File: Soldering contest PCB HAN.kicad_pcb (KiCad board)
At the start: 2 copper layers, 11 parts, among them J1 Screw_Terminal_01x02, Q1 2N3904, Q2 2N3904

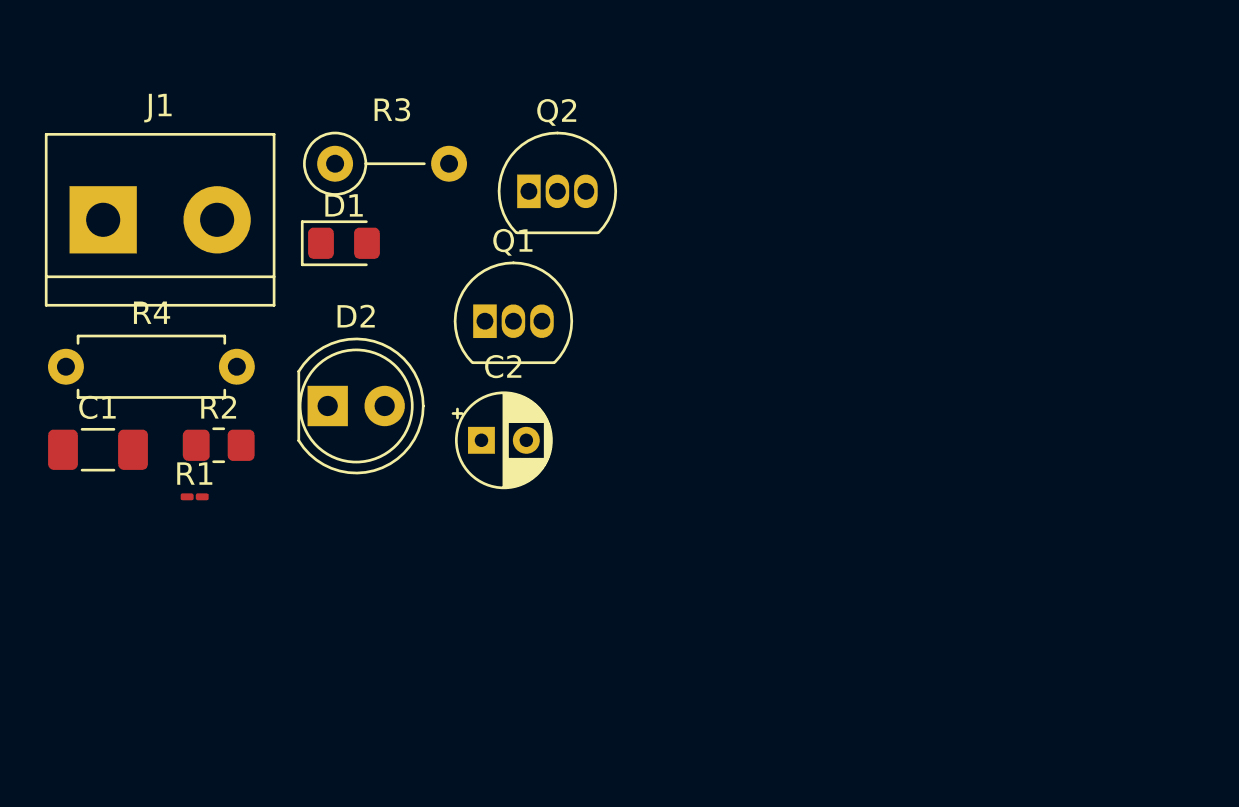
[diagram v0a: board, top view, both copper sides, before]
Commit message: replaced q1 footprint
replaced with sot23 handsolderable
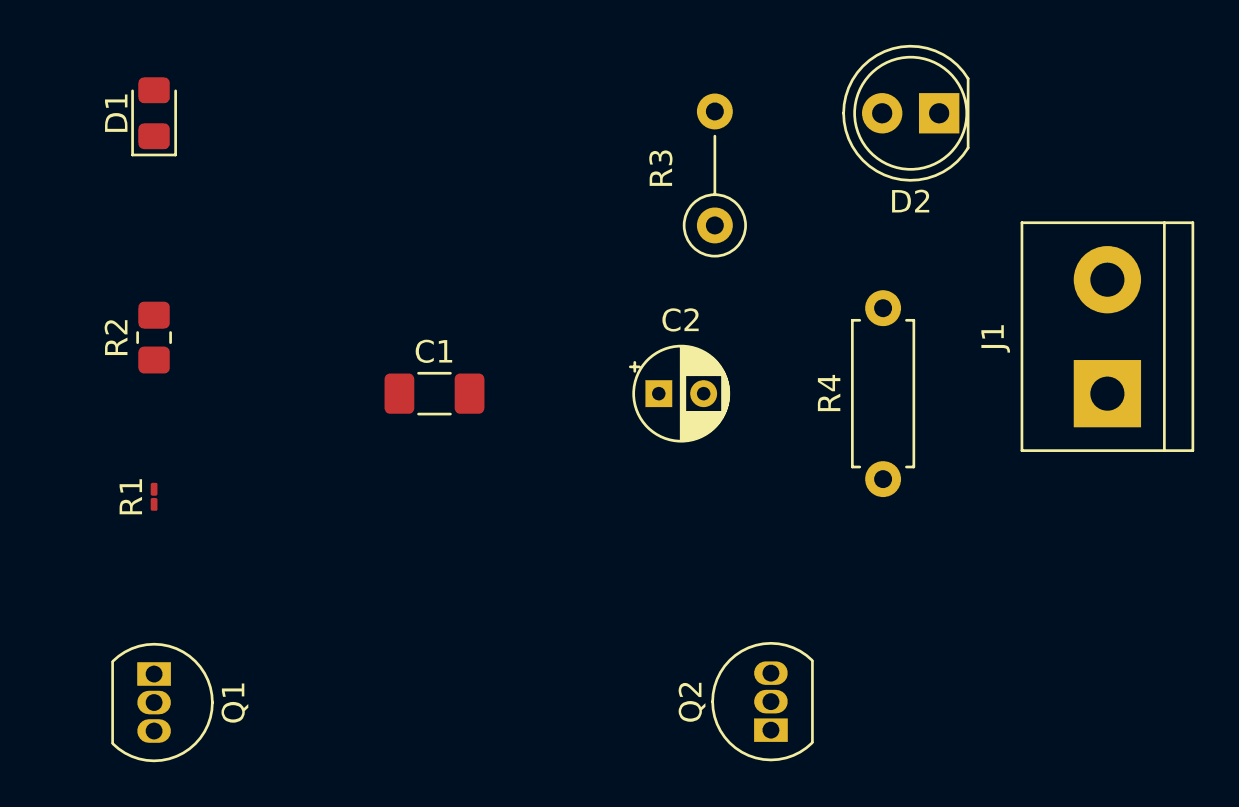
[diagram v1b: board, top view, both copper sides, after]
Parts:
- moved J1 45.4 mm to (175.0, 97.5), turned to 90 degrees
- moved R4 36.8 mm to (165.0, 101.3), turned to 90 degrees
- moved D2 30.2 mm to (167.5, 85.0), turned to 180 degrees
- moved Q2 26.3 mm to (160.0, 112.5), turned to 90 degrees
- moved Q1 21.6 mm to (132.5, 110.0), turned to -90 degrees
- moved R3 17.2 mm to (157.5, 90.0), turned to 90 degrees
- moved C1 15.2 mm to (145.0, 97.5)
- moved D1 10.3 mm to (132.5, 85.0), turned to 90 degrees
- moved C2 8.17 mm to (155.0, 97.5)
- moved R2 5.60 mm to (132.5, 95.0), turned to 90 degrees
- moved R1 1.81 mm to (132.5, 102.1), turned to 90 degrees

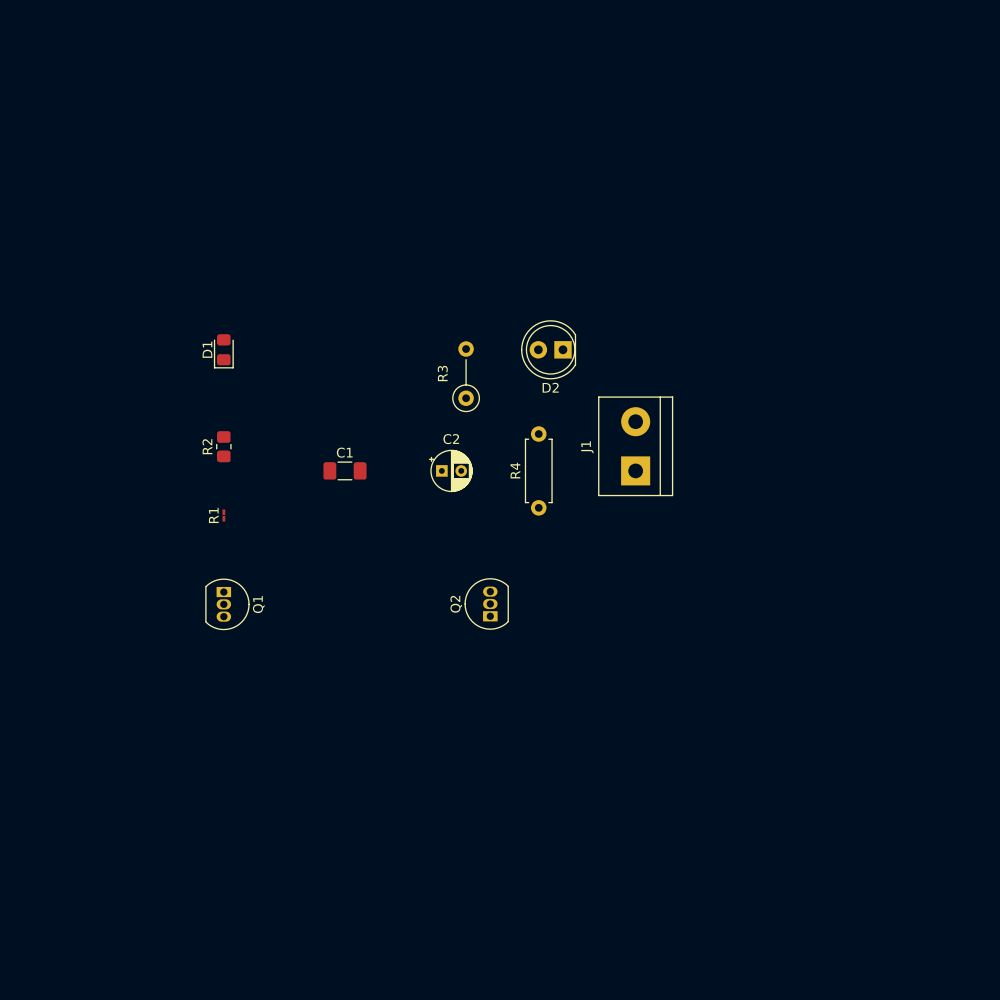
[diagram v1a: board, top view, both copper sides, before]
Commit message: archived 3d model, created general layout
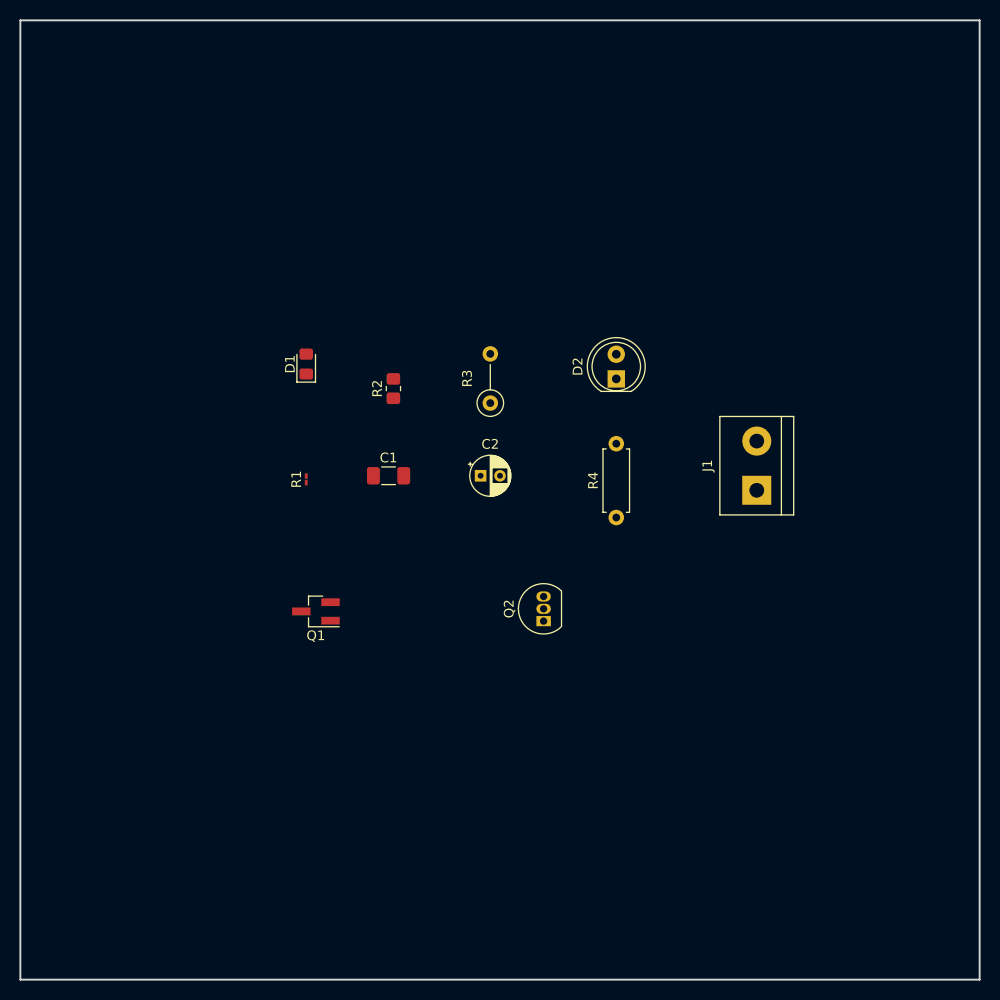
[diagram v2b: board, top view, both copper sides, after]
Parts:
- Q1: footprint Package_TO_SOT_THT:TO-92_Inline -> Package_TO_SOT_SMD:SOT-23_Handsoldering
- moved R2 18.5 mm to (150.0, 89.0)
- moved J1 12.7 mm to (187.5, 99.5)
- moved Q1 9.71 mm to (142.0, 112.0), turned to 180 degrees
- moved R1 9.29 mm to (141.0, 98.4)
- moved D1 8.63 mm to (141.0, 86.5)
- moved R4 8.06 mm to (173.0, 102.3)
- moved D2 6.26 mm to (173.0, 88.0), turned to 90 degrees
- moved Q2 5.52 mm to (165.5, 113.0)
- moved C1 4.53 mm to (149.5, 98.0)
- moved C2 4.03 mm to (159.0, 98.0)
- moved R3 2.55 mm to (160.0, 90.5)
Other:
- board outline added: 99 x 99 mm

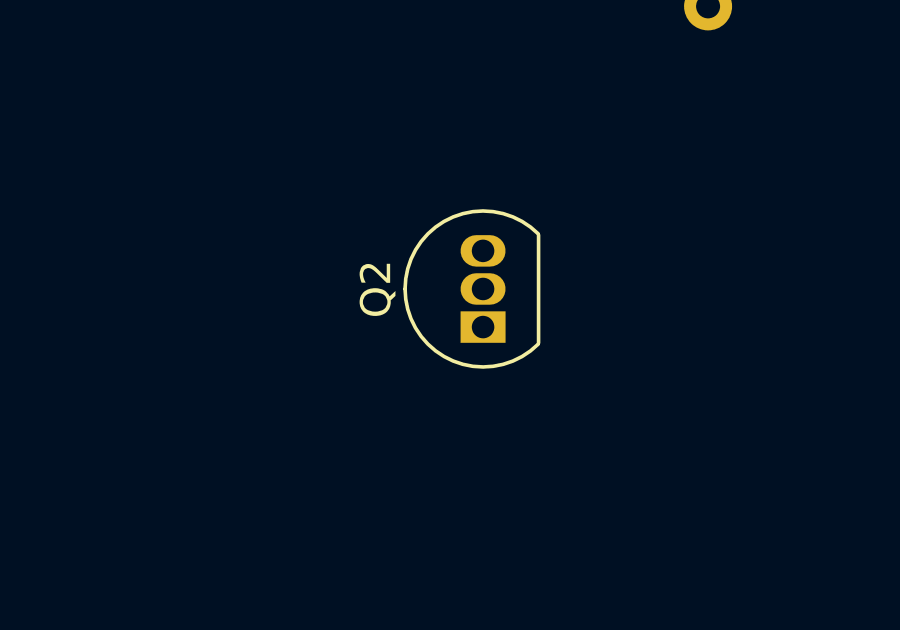
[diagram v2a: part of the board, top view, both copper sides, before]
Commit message: changed Q2 footprint
to to92 wide
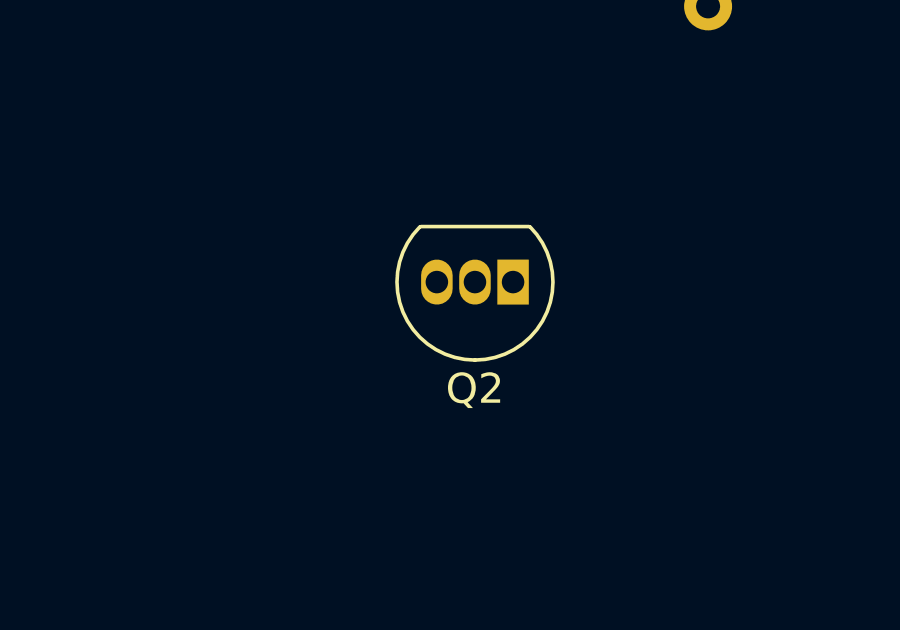
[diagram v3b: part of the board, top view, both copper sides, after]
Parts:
- moved Q2 1.80 mm to (166.5, 111.5), turned to 180 degrees
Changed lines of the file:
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@@
   )
   (footprint "Package_TO_SOT_THT:TO-92_Inline" (layer "F.Cu")
-    (at 165.5 113 90)
+    (at 166.5 111.5 180)
     (descr "TO-92 leads in-line, narrow, oval pads, drill 0.75mm (see NXP sot054_po.pdf)")
     (tags "to-92 sc-43 sc-43a sot54 PA33 transistor")
@@
     (property "Sheetname" "")
     (attr through_hole)
-    (fp_text reference "Q2" (at 1.27 -3.56 90) (layer "F.SilkS")
+    (fp_text reference "Q2" (at 1.27 -3.56) (layer "F.SilkS")
       (effects (font (size 1 1) (thickness 0.15)))
     )
-    (fp_text value "2N3904" (at 1.27 2.79 90) (layer "F.Fab")
+    (fp_text value "2N3904" (at 1.27 2.79) (layer "F.Fab")
       (effects (font (size 1 1) (thickness 0.15)))
     )
-    (fp_text user "${REFERENCE}" (at 1.27 0 90) (layer "F.Fab")
+    (fp_text user "${REFERENCE}" (at 1.27 0) (layer "F.Fab")
       (effects (font (size 1 1) (thickness 0.15)))
     )
@@
     (fp_arc (start 1.27 -2.48) (mid 3.561221 -0.949055) (end 3.023625 1.753625) (layer "F.Fab") (width 0.1))
     (fp_arc (start -0.483625 1.753625) (mid -1.021221 -0.949055) (end 1.27 -2.48) (layer "F.Fab") (width 0.1))
-    (pad "1" thru_hole rect (at 0 0 90) (size 1.05 1.5) (drill 0.75) (layers *.Cu *.Mask)
+    (pad "1" thru_hole rect (at 0 0 180) (size 1.05 1.5) (drill 0.75) (layers *.Cu *.Mask)
       (net 8 "GND") (pinfunction "E") (pintype "passive"))
-    (pad "2" thru_hole oval (at 1.27 0 90) (size 1.05 1.5) (drill 0.75) (layers *.Cu *.Mask)
+    (pad "2" thru_hole oval (at 1.27 0 180) (size 1.05 1.5) (drill 0.75) (layers *.Cu *.Mask)
       (net 2 "Net-(C1-Pad2)") (pinfunction "B") (pintype "passive"))
-    (pad "3" thru_hole oval (at 2.54 0 90) (size 1.05 1.5) (drill 0.75) (layers *.Cu *.Mask)
+    (pad "3" thru_hole oval (at 2.54 0 180) (size 1.05 1.5) (drill 0.75) (layers *.Cu *.Mask)
       (net 3 "Net-(C2-Pad1)") (pinfunction "C") (pintype "passive"))
     (model "${KIPRJMOD}/packages3D/TO-92_Inline.wrl"
